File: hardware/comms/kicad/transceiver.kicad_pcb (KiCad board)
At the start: 4 copper layers, 96 x 90.2 mm, 107 parts, among them J1 Conn_01x20, J2 Conn_01x20, J3 Conn_01x20, J4 Conn_Coaxial_Small, J5 Conn_Coaxial_Small, Q1 NPN, U1 MCP6022, U2 74LVC1G86, U3 PSA4-5043+, U4 ADE-1+, U6 ADL5602ARKZ-R7, Y1 Crystal_GND2, Y2 Si5351A-B-GT

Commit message: Checkpoint comms PCB synchronization and connector alignment
Repair schematic-to-PCB links and apply the native update. Standardize J6/J7/J8 as DNP headers, align CSKB sockets for top-side assembly, and record pad-mapping verification.

Pre-RF-layout checkpoint: retain legacy circuitry for reviewed cleanup. Latest DRC has 631 errors, 273 warnings, and 140 unconnected items; board is not fabrication-ready.
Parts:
- added C55: 3.9p, Capacitor_SMD:C_0402_1005Metric, F.Cu at (0.94, 0.48)
- added C56: 9.1p, Capacitor_SMD:C_0402_1005Metric, F.Cu at (0.94, 2.46)
- added C60: 1.6p, Capacitor_SMD:C_0402_1005Metric, F.Cu at (0.94, 4.42)
- added C64: 9.1p, Capacitor_SMD:C_0402_1005Metric, F.Cu at (0.94, 6.39)
- added C67: 3.9p, Capacitor_SMD:C_0402_1005Metric, F.Cu at (0.94, 8.37)
- added C75: 100n, Capacitor_SMD:C_0402_1005Metric, F.Cu at (3.81, 0.48)
- added C81: 8.2p, Capacitor_SMD:C_0402_1005Metric, F.Cu at (16.5, 0.48)
- added C82: 100n, Capacitor_SMD:C_0402_1005Metric, F.Cu at (3.81, 2.46)
- added C85: 8.2p, Capacitor_SMD:C_0402_1005Metric, F.Cu at (3.81, 4.42)
- added C86: 3.9p, Capacitor_SMD:C_0402_1005Metric, F.Cu at (3.81, 6.39)
- added C87: 9.1p, Capacitor_SMD:C_0402_1005Metric, F.Cu at (16.5, 2.46)
- added C89: 1.6p, Capacitor_SMD:C_0402_1005Metric, F.Cu at (16.5, 4.42)
- added C90: 9.1p, Capacitor_SMD:C_0402_1005Metric, F.Cu at (3.81, 8.37)
- added C91: 1.6p, Capacitor_SMD:C_0402_1005Metric, F.Cu at (6.67, 0.48)
- added C92: 9.1p, Capacitor_SMD:C_0402_1005Metric, F.Cu at (16.5, 6.39)
- added C94: 3.9p, Capacitor_SMD:C_0402_1005Metric, F.Cu at (16.5, 8.37)
- added C95: 9.1p, Capacitor_SMD:C_0402_1005Metric, F.Cu at (6.67, 2.46)
- added C97: 3.9p, Capacitor_SMD:C_0402_1005Metric, F.Cu at (6.67, 4.42)
- added C98: 1.6p, Capacitor_SMD:C_0402_1005Metric, F.Cu at (16.5, 10.3)
- added L12: 10n, Inductor_SMD:L_0402_1005Metric, F.Cu at (9.56, 4.95)
- added L13: 10n, Inductor_SMD:L_0402_1005Metric, F.Cu at (9.56, 6.93)
- added L18: 15n, Inductor_SMD:L_0402_1005Metric, F.Cu at (9.56, 8.93)
- added L20: 10n, Inductor_SMD:L_0402_1005Metric, F.Cu at (9.56, 10.9)
- added L22: 10n, Inductor_SMD:L_0402_1005Metric, F.Cu at (9.56, 12.9)
- added Q4: 2SC3356, Package_TO_SOT_SMD:SOT-23, F.Cu at (10.6, 1.73)
- added R33: 47k, Resistor_SMD:R_0402_1005Metric, F.Cu at (9.56, 14.9)
- added U5: MCP6022, Package_SO:SOIC-8_3.9x4.9mm_P1.27mm, F.Cu at (3.73, 12.7)
- C100: renamed from C13; value 6.8p -> 9.1p
- C101: renamed from C11; value 10p -> 3.9p
- C58: renamed from C43; footprint Vault:FP-EEH-D-MFG -> Ember_RF:CP_Elec_Panasonic_D_6.3x5.8
- C59: renamed from C49; footprint Vault:FP-EEH-D-MFG -> Ember_RF:CP_Elec_Panasonic_D_6.3x5.8
- C83: renamed from C33; value 100n -> 1n
- C84: renamed from C9; value 10p -> 3.9p
- C93: renamed from C10; value 10p -> 3.9p
- C96: renamed from C12; value 6.8p -> 9.1p
- H3: renamed from H1; footprint Vault:SAMTEC_ESQ-126-37-G-D -> Ember_RF:Samtec_ESQ-126-39-G-D_2x26_P2.54mm
- H4: renamed from H2; footprint Vault:SAMTEC_ESQ-126-37-G-D -> Ember_RF:Samtec_ESQ-126-39-G-D_2x26_P2.54mm
- J6: renamed from J1; footprint Vault:FP-ESQ-120-14-G-S-MFG -> Connector_PinHeader_2.54mm:PinHeader_1x20_P2.54mm_Vertical
- J7: renamed from J2; footprint Vault:FP-ESQ-120-14-G-S-MFG -> Connector_PinHeader_2.54mm:PinHeader_1x20_P2.54mm_Vertical
- J8: renamed from J3; footprint Vault:FP-ESQ-120-14-G-S-MFG -> Connector_PinHeader_2.54mm:PinHeader_1x20_P2.54mm_Vertical
- L17: renamed from L1; value 220n -> 15n; footprint Inductor_SMD:L_0805_2012Metric -> Inductor_SMD:L_0402_1005Metric
- L19: renamed from L7; value 15n -> 10n
- L21: renamed from L8; value 15n -> 10n
- L23: renamed from L3; value 15n -> 10n
- L24: renamed from L4; value 15n -> 10n
- Q3: renamed from Q1; value NPN -> 2SC3356
- R3: renamed from R1; footprint Vault:RESC1005X40X25NL05T10 -> Resistor_SMD:R_0402_1005Metric
- R4: renamed from R2; footprint Vault:RESC1005X40X25NL05T10 -> Resistor_SMD:R_0402_1005Metric
- TP11: renamed from TP3; footprint Vault:TP06R -> TestPoint:TestPoint_Pad_D1.0mm
- TP12: renamed from TP4; footprint Vault:TP06R -> TestPoint:TestPoint_Pad_D1.0mm
- TP13: renamed from TP5; footprint Vault:TP06R -> TestPoint:TestPoint_Pad_D1.0mm
- TP14: renamed from TP6; footprint Vault:TP06R -> TestPoint:TestPoint_Pad_D1.0mm
- TP15: renamed from TP7; footprint Vault:TP06R -> TestPoint:TestPoint_Pad_D1.0mm
- TP16: renamed from TP8; footprint Vault:TP06R -> TestPoint:TestPoint_Pad_D1.0mm
- U7: renamed from U2; footprint Vault:FP-DBV0005A-MFG -> Package_TO_SOT_SMD:SOT-23-5
- U9: renamed from U3; footprint Package_TO_SOT_SMD:SOT-343_SC-70-4 -> Ember_RF:PSA4-5043_MMM1362
- moved H4 31.8 mm to (106.9, 104.4), turned to 180 degrees
- moved H3 31.8 mm to (111.9, 104.4), turned to 180 degrees
- moved J6 24.1 mm to (184.6, 96.1), turned to -90 degrees
- moved J7 24.1 mm to (184.6, 113.9), turned to -90 degrees
- moved J8 24.1 mm to (190.5, 129.1), turned to 180 degrees
- renumbered C4 to C2, C5 to C3, C6 to C4, C7 to C5, C39 to C57, C2 to C6, C42 to C61, C48 to C62, C40 to C63, C25 to C65, C15 to C66, C50 to C68, C38 to C69, C3 to C7, C51 to C70, C17 to C71, C41 to C72, C14 to C73, C52 to C74, C18 to C76, C35 to C77, C53 to C78, C27 to C79, C16 to C80, C44 to C88, C34 to C99, D6 to D10, D7 to D11, D3 to D12, D4 to D13, D2 to D14, D1 to D8, D5 to D9, J4 to J9, L5 to L15, L14 to L16, L12 to LEGACY_L12, L13 to LEGACY_L13, R3 to R1, R4 to R2, R11 to R20, R12 to R21, R14 to R22, R15 to R23, R16 to R24, R6 to R25, R17 to R26, R5 to R27, R10 to R28, R13 to R29, R9 to R30, R18 to R31, R8 to R32, R7 to R34, U4 to U10, U6 to U8
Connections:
- net /3V3_IND renamed /Digital Control/3V3_IND
- net /ADC_VREF renamed /Digital Control/ADC_VREF
- net /CLK0_OUT renamed CLK0_OUT
- net /CLK1_OUT renamed CLK1_OUT
- net /COMMS_IRQ renamed COMMS_IRQ
- net /GPIO0 renamed /Digital Control/GPIO0
- net /GPIO1 renamed /Digital Control/GPIO1
- net /GPIO13 renamed /Digital Control/GPIO13
- net /GPIO14 renamed /Digital Control/GPIO14
- net /GPIO15 renamed /Digital Control/GPIO15
- net /GPIO22 renamed /Digital Control/GPIO22
- net /RUN_RESET renamed /Digital Control/RUN_RESET
- net /RX_ACTIVE renamed /Digital Control/RX_ACTIVE
- net /RX_IF renamed RX_IF
- net /SPI_COMMS_CS_N renamed SPI_COMMS_CS_N
- net /SPI_COMMS_MISO renamed SPI_COMMS_MISO
- net /SPI_COMMS_MOSI renamed SPI_COMMS_MOSI
- net /SPI_COMMS_SCK renamed SPI_COMMS_SCK
- net /TX_437 renamed TX_437
- net /TX_ACTIVE renamed /Digital Control/TX_ACTIVE
- net /VBAT renamed /Connectors/VBAT
- C100 pad 1: Net-(C11-Pad1) -> Net-(C100-Pad1)
- C101 pad 1: Net-(C11-Pad1) -> Net-(C100-Pad1)
- C57 pad 2: Net-(U1A--) -> Net-(U5A--)
- C63 pad 1: Net-(U1A-+) -> Net-(U5A-+)
- C69 pad 1: Net-(U1B-+) -> Net-(U5B-+)
- C69 pad 2: Net-(U1A--) -> Net-(U5A--)
- C72 pad 2: Net-(U1B-+) -> Net-(U5B-+)
- C73 pad 1: Net-(Q1-B) -> Net-(Q3-B)
- C73 pad 2: /BPSK_145 -> /TX Chain/RF_TX_BPSK_145
- C83 pad 1: Net-(C22-Pad1) -> Net-(Q4-B)
- C84 pad 2: Net-(C20-Pad1) -> Net-(C84-Pad2)
- C93 pad 1: /TRIPLER_OUT -> TRIPLER_OUT
- C93 pad 2: Net-(C10-Pad2) -> Net-(C93-Pad2)
- C96 pad 1: Net-(C10-Pad2) -> Net-(C93-Pad2)
- D14 pad 1: /PICO_VSYS -> PICO_VSYS
- J7 pad 14: /I2C_SCL -> I2C_SCL
- J7 pad 15: /I2C_SDA -> I2C_SDA
- J7 pad 2: /PICO_VSYS -> PICO_VSYS
- J7 pad 20: /BPSK_DATA -> BPSK_DATA
- J7 pad 9: /RX_BASEBAND -> RX_BASEBAND
- J9 pad 1: /TX_OUT -> ANT
- L16 pad 2: Net-(U4-RF) -> Net-(U9-OUT_DC)
- L17 pad 2: /TRIPLER_OUT -> TRIPLER_OUT
- L19 pad 1: Net-(C20-Pad1) -> Net-(C84-Pad2)
- L21 pad 1: Net-(C19-Pad1) -> Net-(C89-Pad2)
- L23 pad 1: Net-(C10-Pad2) -> Net-(C93-Pad2)
- L24 pad 1: Net-(C11-Pad1) -> Net-(C100-Pad1)
- Q3 pad 1: /TRIPLER_OUT -> Net-(Q3-B)
- Q3 pad 2: Net-(Q1-B) -> GND
- Q3 pad 3: GND -> TRIPLER_OUT
- R1 pad 2: /I2C_SDA -> I2C_SCL
- R2 pad 2: /I2C_SCL -> I2C_SDA
- R21 pad 2: Net-(U1A-+) -> Net-(U5A-+)
- R25 pad 1: /BPSK_DATA -> BPSK_DATA
- R27 pad 1: Net-(Q1-B) -> Net-(Q3-B)
- R30 pad 1: Net-(U1B--) -> Net-(U5B--)
- R32 pad 1: Net-(U1B--) -> Net-(U5B--)
- R32 pad 2: /RX_BASEBAND -> RX_BASEBAND
- TP12 pad 1: /BPSK_145 -> BPSK_DATA
- TP13 pad 1: /TRIPLER_OUT -> TRIPLER_OUT
- TP16 pad 1: /RX_BASEBAND -> RX_BASEBAND
- U10 pad 3: Net-(U4-RF) -> Net-(U10-RF)
- U10 pad 6: Net-(U4-LO) -> Net-(U10-LO)
- U7 pad 4: /BPSK_145 -> /TX Chain/RF_TX_BPSK_145
- U9 pad 1: Net-(C30-Pad2) -> Net-(U9-OUT_DC)
- U9 pad 3: Net-(U4-RF) -> Net-(U9-IN)
- U9 pad 4: (no net) -> GND
- Y2 pad 4: /I2C_SCL -> I2C_SCL
- Y2 pad 5: /I2C_SDA -> I2C_SDA
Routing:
- net (no net): track 0.00 -> 38.1 mm
- net GND: track 23.0 -> 58.7 mm
- net +5V: track 10.4 -> 32.4 mm, vias 13 -> 9
- net RX_BASEBAND: track 0.00 -> 14.5 mm
- net /RX_BASEBAND: track 14.5 -> 0.00 mm
- net +5V_CON: track 15.5 -> 1.93 mm
- net Net-(U10-IF): track 12.4 -> 0.00 mm
- net +3V3: track 25.9 -> 15.1 mm
- net Net-(U1A--): track 10.6 -> 1.21 mm
- net Net-(U5A--): track 0.00 -> 9.36 mm
- net NetC38_1: track 8.43 -> 0.00 mm
- net NetC4_2: track 8.18 -> 0.00 mm
- net NetC10_2: track 5.64 -> 0.00 mm
- net NetC9_2: track 5.53 -> 0.00 mm
- net NetC1_2: track 5.09 -> 0.00 mm
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- added copper zone on F.Cu, net Net-(Q3-B)
- removed copper zone on F.Cu, net Net-(Q1-B)

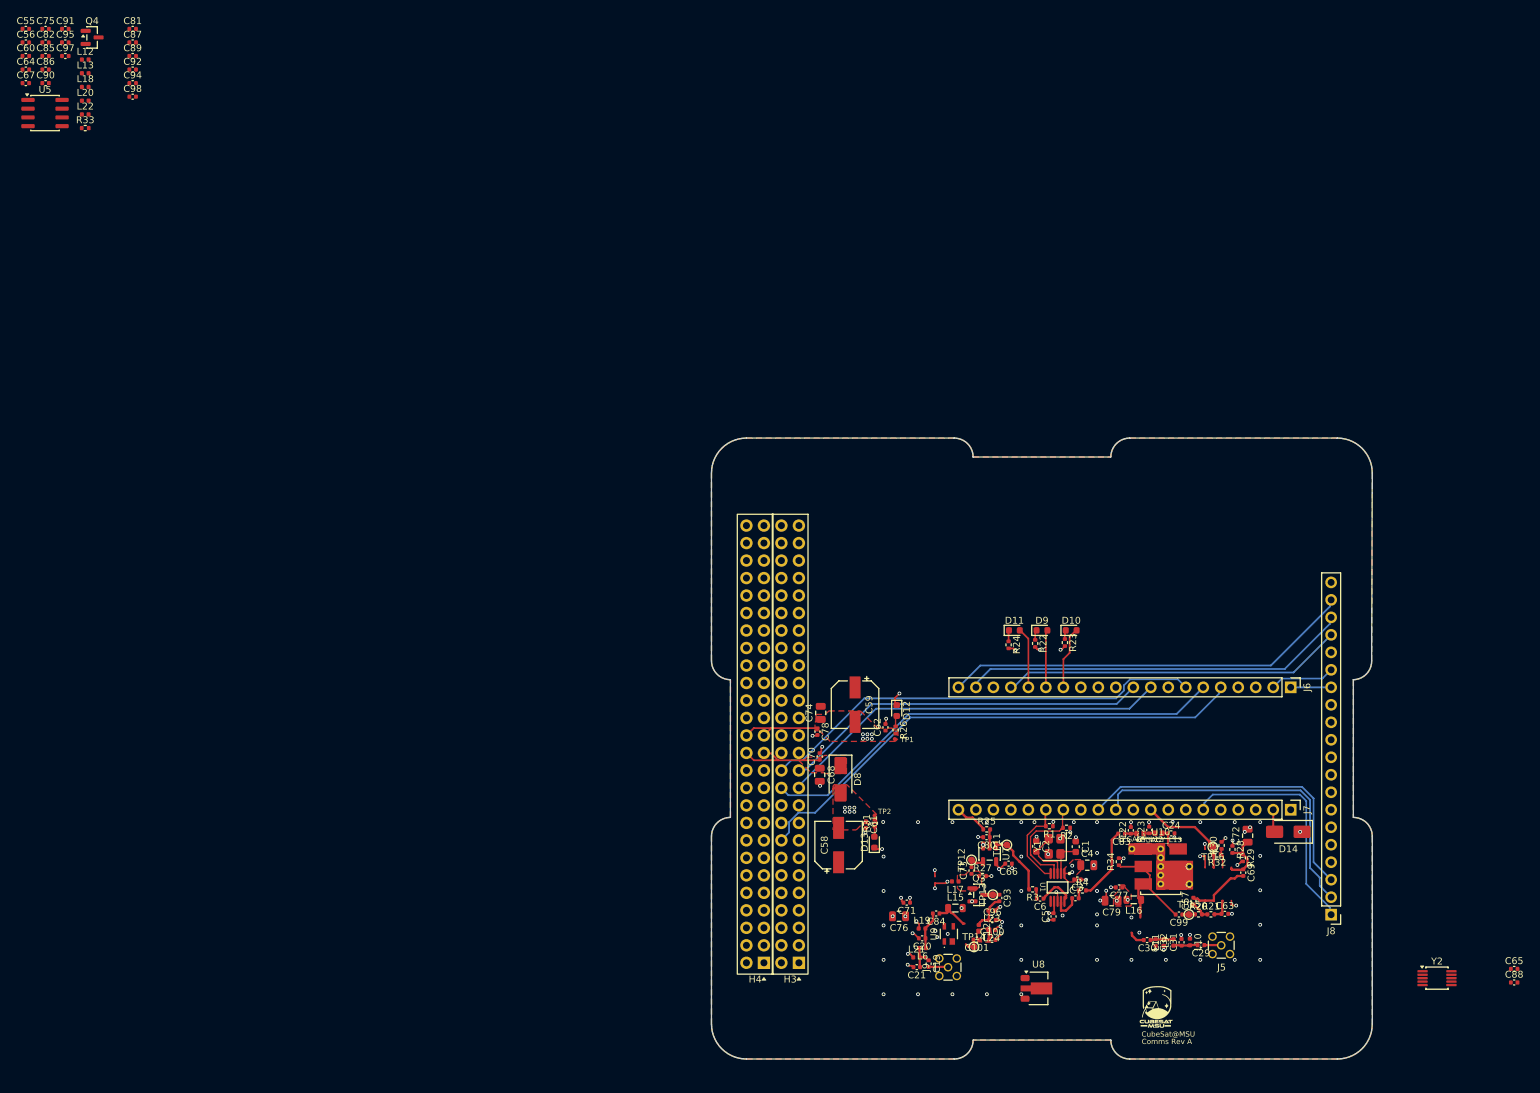
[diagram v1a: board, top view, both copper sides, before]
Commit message: Checkpoint validated single-antenna comms routing before placement optimization
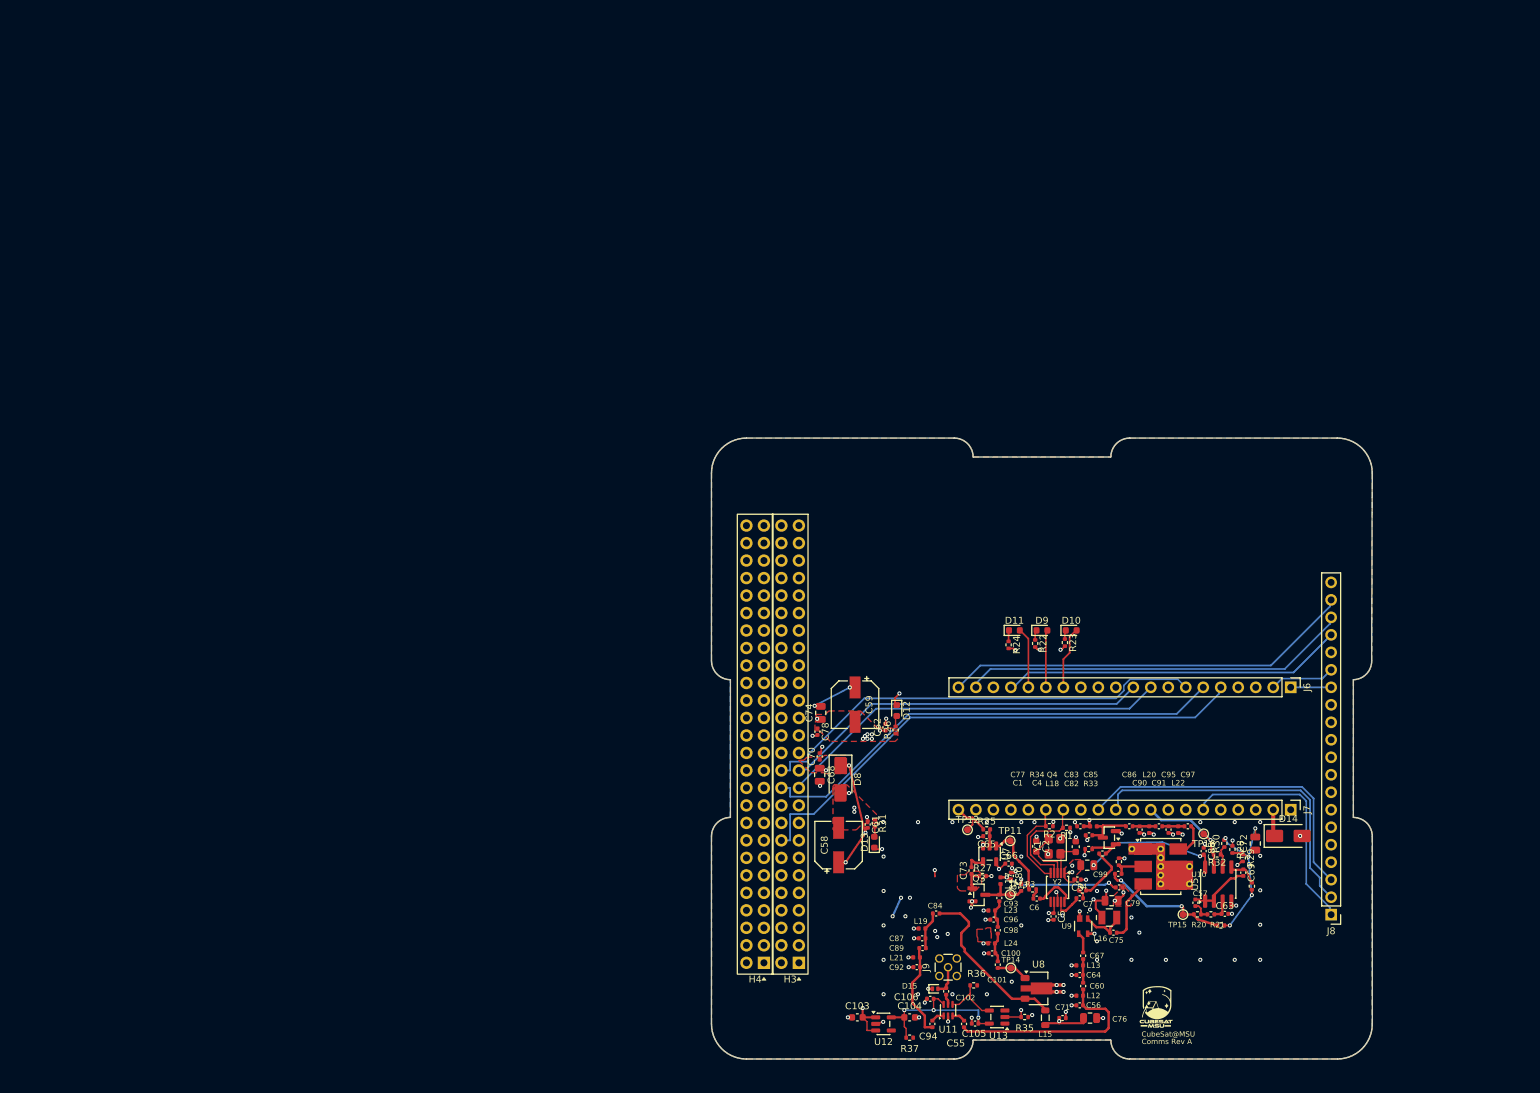
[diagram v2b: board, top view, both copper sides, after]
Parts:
- removed C19, C22, C24, C29, C30, C31, C32: 10p, Capacitor_SMD:C_0402_1005Metric
- removed C20, C21: 6.8p, Capacitor_SMD:C_0402_1005Metric
- removed C23: 33p, Capacitor_SMD:C_0402_1005Metric
- removed J5: Conn_Coaxial_Small, Connector_Coaxial:MMCX_Molex_73415-1471_Vertical
- removed L10, L11, L9: 82n, Inductor_SMD:L_0402_1005Metric
- removed L2, L6: 15n, Inductor_SMD:L_0402_1005Metric
- removed LEGACY_L12, LEGACY_L13: 68n, Vault:Chip2PinSM127P600-8N
- removed TP1, TP2: TestPoint, Vault:TP06R
- removed U1: MCP6022, Vault:SLAB-MSOP-10_N
- added C102: 100p, Capacitor_SMD:C_0402_1005Metric, F.Cu at (134.6, 140.3)
- added C103: 1u, Capacitor_SMD:C_0603_1608Metric, F.Cu at (121.7, 144.1)
- added C104: 1u, Capacitor_SMD:C_0603_1608Metric, F.Cu at (129.3, 144.1)
- added C105: 100n, Capacitor_SMD:C_0402_1005Metric, F.Cu at (138.8, 144.9)
- added C106: 100n, Capacitor_SMD:C_0402_1005Metric, F.Cu at (132.3, 141.3)
- added D15: PESD5V0F1BRLD, Diode_SMD:D_SOD-882D, F.Cu at (133.0, 139.9)
- added R35: 10k, Resistor_SMD:R_0402_1005Metric, F.Cu at (146.0, 144.0)
- added R36: 10k, Resistor_SMD:R_0402_1005Metric, F.Cu at (138.6, 139.4)
- added R37: 10k, Resistor_SMD:R_0402_1005Metric, F.Cu at (129.3, 147.0)
- added R38: 100k, R_0402_1005Metric, F.Cu at (174.5, 130.7)
- added R39: 100k, R_0402_1005Metric, F.Cu at (179.0, 125.0)
- added U11: PE4259, Package_TO_SOT_SMD:SOT-363_SC-70-6, F.Cu at (134.9, 143.0)
- added U12: TLV75530PDBVR, Package_TO_SOT_SMD:SOT-23-5, F.Cu at (125.5, 145.0)
- added U13: SN74LVC1G17DBVR, Package_TO_SOT_SMD:SOT-23-5, F.Cu at (142.0, 144.0)
- L16: value 1u -> 220n; footprint Inductor_SMD:L_0805_2012Metric -> Ember_RF:L_Coilcraft_0805HP
- Y1: value Crystal_GND2 -> 25MHz
- moved C56 207.3 mm to (154.0, 142.3), turned to 180 degrees
- moved C60 204.5 mm to (154.5, 139.5), turned to 90 degrees
- moved U5 203.9 mm to (174.1, 124.7), turned to 90 degrees
- moved C75 203.2 mm to (158.9, 131.8)
- moved C64 201.8 mm to (154.0, 137.9), turned to 180 degrees
- moved C67 199.1 mm to (154.5, 135.1), turned to 90 degrees
- moved C55 198.6 mm to (137.2, 145.0), turned to -90 degrees
- moved L12 198.4 mm to (154.0, 140.9), turned to 180 degrees
- moved C97 197.7 mm to (169.7, 116.3)
- moved C95 196.8 mm to (166.9, 116.8), turned to -90 degrees
- moved C91 196.6 mm to (165.5, 116.3)
- moved L13 194.0 mm to (154.0, 136.5), turned to 180 degrees
- moved C90 192.4 mm to (162.7, 116.8), turned to -90 degrees
- moved C86 192.0 mm to (161.2, 116.3)
- moved L22 189.7 mm to (168.3, 116.8), turned to -90 degrees
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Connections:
- net /Digital Control/TX_ACTIVE renamed TX_ACTIVE
- C69 pad 1: Net-(U5B-+) -> /RX Chain/RX_AMP_IN
- C72 pad 2: Net-(U5B-+) -> /RX Chain/VREF_RX
- R28 pad 2: Net-(R28-Pad2) -> /RX Chain/VREF_RX
- R29 pad 1: Net-(R28-Pad2) -> /RX Chain/VREF_RX
- R30 pad 2: GND -> /RX Chain/VREF_RX
- U5 pad 5: Net-(U5B-+) -> /RX Chain/RX_AMP_IN
- Y1 pad 4: (no net) -> GND
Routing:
- net +5V: track 32.4 -> 193.0 mm, vias 9 -> 15
- net +3V3: track 15.1 -> 125.0 mm
- net TX_ACTIVE: track 9.22 -> 71.2 mm, vias 0 -> 1
- net (no net): track 38.1 -> 0.00 mm
- net Net-(C55-Pad2): track 0.00 -> 30.3 mm
- net /RX Chain/VREF_RX: track 0.00 -> 25.3 mm, vias 0 -> 5
- net Net-(C84-Pad1): track 0.00 -> 25.1 mm, vias 2 -> 0
- net +3V0: track 0.00 -> 23.7 mm, vias 0 -> 3
- net +5V_CON: track 1.93 -> 24.8 mm, vias 2 -> 3
- net RX_IF: track 1.98 -> 18.8 mm, vias 0 -> 2
- net Net-(C89-Pad2): track 1.05 -> 13.8 mm, vias 1 -> 0
- net Net-(U10-RF): track 0.00 -> 9.21 mm
- net /Single Antenna RF Switch/SW_CTRL_3V0: track 0.00 -> 8.64 mm
- net Net-(Y2-XB): track 0.00 -> 8.18 mm
- net Net-(Q4-C): track 0.00 -> 7.75 mm
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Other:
- outline, holes or cut-outs redrawn

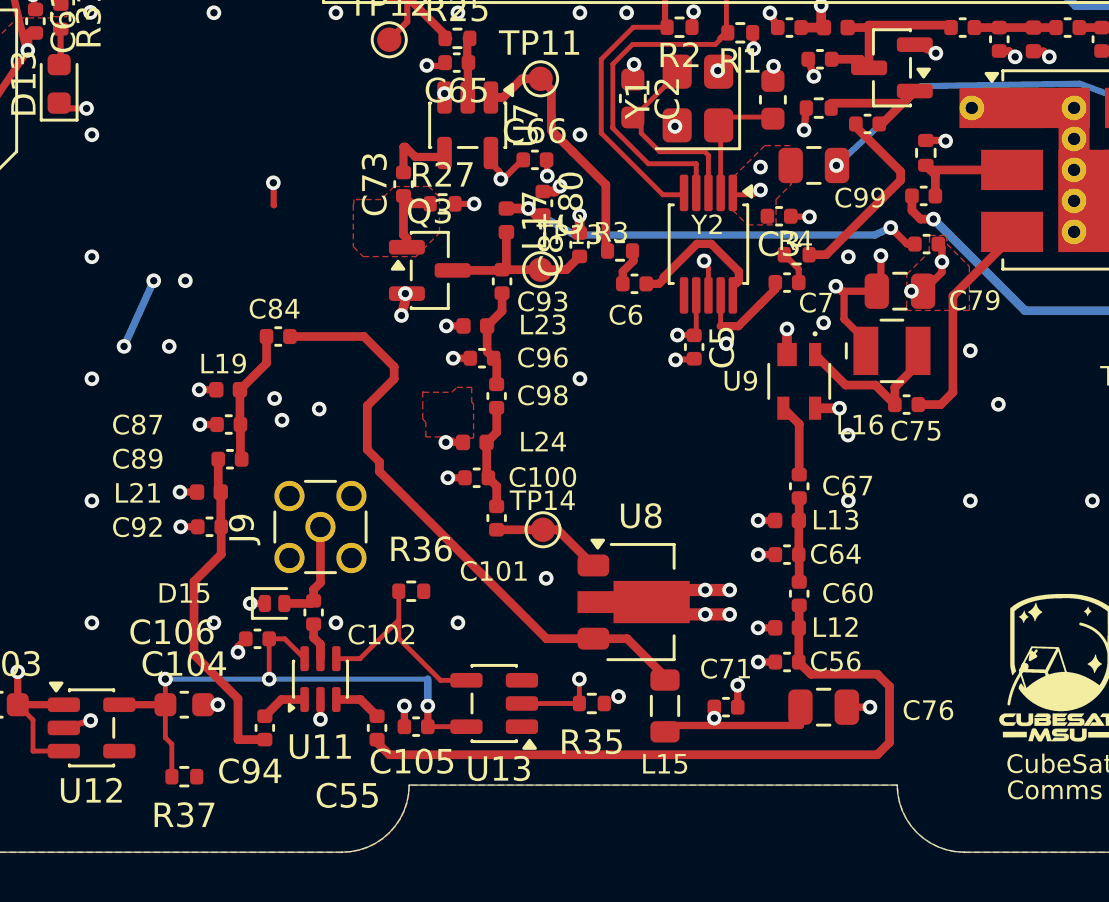
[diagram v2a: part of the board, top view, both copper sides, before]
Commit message: Checkpoint compact TX and RX placement with validated routing
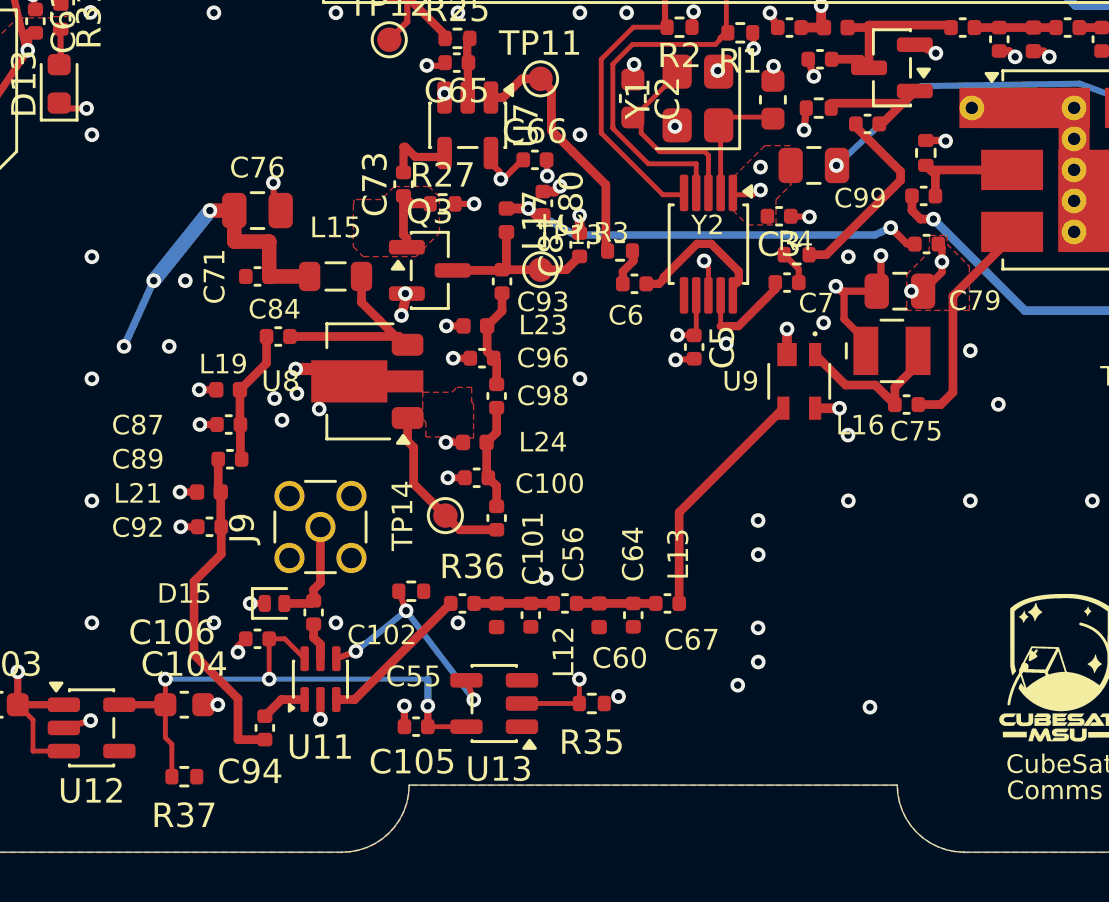
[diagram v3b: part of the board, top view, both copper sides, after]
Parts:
- moved C76 30.9 mm to (132.3, 123.8)
- moved C71 26.1 mm to (132.3, 126.5), turned to 0 degrees
- moved L15 22.2 mm to (135.5, 126.5), turned to 0 degrees
- moved U8 14.6 mm to (136.5, 130.8), turned to 180 degrees
- moved L12 11.9 mm to (142.1, 140.4), turned to -90 degrees
- moved C56 10.7 mm to (143.5, 140.4), turned to -90 degrees
- moved C60 9.61 mm to (144.9, 139.9), turned to 0 degrees
- moved L13 8.62 mm to (146.3, 140.4), turned to -90 degrees
- moved C67 7.22 mm to (149.1, 139.9), turned to 0 degrees
- moved C64 6.77 mm to (147.7, 140.4), turned to -90 degrees
- moved C55 6.19 mm to (140.7, 139.9), turned to 0 degrees
- moved TP14 4.04 mm to (140.0, 136.3)
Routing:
- net Net-(C55-Pad2): track 30.3 -> 3.24 mm
- net Net-(C84-Pad1): track 25.1 -> 8.63 mm
- net GND: track 52.2 -> 44.6 mm, vias 108 -> 106
- net Net-(U9-IN): track 2.99 -> 9.77 mm
- net RX_IN: track 1.95 -> 6.32 mm
- net +5V: track 193.0 -> 195.8 mm
- net TX_437: track 4.57 -> 6.98 mm
- net /Single Antenna RF Switch/SW_CTRL_3V0: track 8.64 -> 9.79 mm, vias 0 -> 3
